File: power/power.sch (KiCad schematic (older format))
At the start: 74 parts, among them J1 Conn_01x02_Female, J2 Conn_01x02_Female, J3 CONN_02X03, J4 Conn_01x06_Female, Q1 BS170, Q11 BS170, Q12 BSB014N04LX3, Q2 BS170, Q3 BS170, Q5 BS170, Q6 BS170, Q7 BS170, U1 MAX1648, U2 TPS2592xx

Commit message: rev1 layout organization
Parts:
- removed J4, J?: Conn_01x06_Female, Connector_PinHeader_1.00mm:PinHeader_1x06_P1.00mm_Vertical, symbol Connector:Conn_01x06_Female
- added J12, J13, J14, J15, J4, J5: Conn_01x02_Female, Connector_PinHeader_1.00mm:PinHeader_1x02_P1.00mm_Vertical, symbol Connector:Conn_01x02_Female
- added TH?: Thermistor_NTC, symbol Device:Thermistor_NTC
- gave numbers to parts that had none: 22

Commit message: thermistor footprint
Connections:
- net labels removed: Discharge, SafetySwitchA, SafetySwitchB
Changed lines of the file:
@@
 Text Label 9880 2500 0    50   ~ 0
 FET1A
-Text Label 9880 3500 0    50   ~ 0
-Discharge
 Text Label 9880 2400 0    50   ~ 0
 FET2A
@@
 	1    0    0    -1
 $EndComp
-Text Label 9880 2300 0    50   ~ 0
-SafetySwitchA
 Text Label 9880 3200 0    50   ~ 0
 RESET
@@
 	5650 7170 5650 7370
 Connection ~ 5650 7370
-Text Label 9880 2900 0    50   ~ 0
-SafetySwitchB
 Text Notes 1730 3200 0    50   ~ 0
 1/10 W

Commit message: removed extra thermistor
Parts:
- removed TH?: Thermistor_NTC, symbol Device:Thermistor_NTC
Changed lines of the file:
@@
 	1    0    0    -1
 $EndComp
-$Comp
-L Device:Thermistor_NTC TH?
-U 1 1 5FFA8A9D
-P 4610 820
-F 0 "TH?" V 4320 820 50  0000 C CNN
-F 1 "Thermistor_NTC" V 4411 820 50  0000 C CNN
-F 2 "" H 4610 870 50  0001 C CNN
-F 3 "~" H 4610 870 50  0001 C CNN
-	1    4610 820
-	0    1    1    0
-$EndComp
 $EndSCHEMATC

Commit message: separated charging from main board
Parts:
- removed C10: 0.1uF, Capacitor_SMD:C_0805_2012Metric_Pad1.15x1.40mm_HandSolder, symbol Device:C_Small
- removed C11: 47uF, Capacitor_SMD:C_0805_2012Metric_Pad1.15x1.40mm_HandSolder, symbol Device:CP
- removed C2, C4: 0.1uF, Capacitor_SMD:C_0805_2012Metric_Pad1.15x1.40mm_HandSolder, symbol Device:C
- removed C3: 47nF, Capacitor_SMD:C_0805_2012Metric_Pad1.15x1.40mm_HandSolder, symbol Device:C
- removed C8: 22uF, Capacitor_SMD:C_0805_2012Metric_Pad1.15x1.40mm_HandSolder, symbol Device:CP
- removed C9: 1uF, Capacitor_SMD:C_0805_2012Metric_Pad1.15x1.40mm_HandSolder, symbol Device:C
- removed D3, D5, D6: S, footprints:SD103AW-13-F, symbol Device:D_Schottky
- removed D4: UF5400, Diode_THT:D_DO-201AD_P15.24mm_Horizontal, symbol Diode:UF5400
- removed D7: 12.5V, symbol Device:D_Zener
- removed J2: Conn_01x02_Female, Connector_PinHeader_1.00mm:PinHeader_1x02_P1.00mm_Vertical, symbol Connector:Conn_01x02_Female
- removed L1: 22uH, Inductor_SMD:L_0805_2012Metric_Pad1.15x1.40mm_HandSolder, symbol pspice:INDUCTOR
- removed Q11: BS170, Package_TO_SOT_THT:TO-92_Inline, symbol Transistor_FET:BS170
- removed Q12: BSB014N04LX3, Package_DirectFET:DirectFET_MX, symbol Transistor_FET:BSB014N04LX3
- removed R1, R2, R3, R4: R, Resistor_SMD:R_0805_2012Metric_Pad1.15x1.40mm_HandSolder, symbol Device:R
- removed R13, R5, R6: 10k, Resistor_SMD:R_0805_2012Metric_Pad1.15x1.40mm_HandSolder, symbol Device:R
- removed R15: 10, Resistor_SMD:R_0805_2012Metric_Pad1.15x1.40mm_HandSolder, symbol Device:R
- removed R22: 0.74, Resistor_SMD:R_0805_2012Metric_Pad1.15x1.40mm_HandSolder, symbol Device:R
- removed SW1: SW_Push, symbol Switch:SW_Push
- removed TH4: Thermistor, footprints:Thermistor, symbol Device:Thermistor
- removed U1: MAX1648, Package_SO:SOIC-16_3.9x9.9mm_P1.27mm, symbol Battery_Management:MAX1648
- added D3: D_Zener_13V, footprints:D_13V_Zener, symbol formula:D_Zener_13V
- added J2: Barrel_jack, footprints:barrel_jack_PJ-037A, symbol formula:Barrel_jack
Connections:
- net labels removed: DC+, DC-
- wire segments 187 -> 113
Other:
- note added: "Charging INPUT Connectors"
- note removed: "0V"
- note removed: "1.024V"
- note removed: "1.025V"
- note removed: "1/10 W"
- note removed: "10V"
- note removed: "20V"
- note removed: "3.9V"
- note removed: "35V"
- note removed: "40V"
- note removed: "Charging\n"
- note removed: "Power INPUT Connectors"
- moved on the sheet: J1, J10, J11, J12, J13, J14, J15, J3, J4, J5, J6, J7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

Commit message: half layout
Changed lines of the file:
@@
 Text Label 870  8370 2    50   ~ 0
 BAT-
-Text Label 3740 2500 0    50   ~ 0
+Text Label 3740 3400 0    50   ~ 0
 FET1A
 Text Label 3740 2400 0    50   ~ 0
 FET2A
-Text Label 3740 1700 0    50   ~ 0
+Text Label 3740 2500 0    50   ~ 0
 FET3A
 Text Label 3740 1800 0    50   ~ 0
 FET1B
-Text Label 3740 3400 0    50   ~ 0
+Text Label 3740 1700 0    50   ~ 0
 FET2B
 Text Label 3740 3300 0    50   ~ 0

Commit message: complete layout
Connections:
- net labels removed: VCC
- no-connect marks 6 -> 8
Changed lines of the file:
@@
 MOSI
-$Comp
-L power:VCC #PWR0101
-U 1 1 5E15CCC8
-P 6310 1400
-F 0 "#PWR0101" H 6310 1250 50  0001 C CNN
-F 1 "VCC" H 6327 1573 50  0000 C CNN
-F 2 "" H 6310 1400 50  0001 C CNN
-F 3 "" H 6310 1400 50  0001 C CNN
-	1    6310 1400
-	1    0    0    -1
-$EndComp
 $Comp
 L power:GND #PWR0102
@@
 	1    0    0    -1
 $EndComp
-Text Label 3740 3700 0    50   ~ 0
+Text Label 3740 3500 0    50   ~ 0
 V2A
-Text Label 3740 1600 0    50   ~ 0
+Text Label 3740 2500 0    50   ~ 0
 V3A
-Text Label 3740 1900 0    50   ~ 0
+Text Label 3740 2000 0    50   ~ 0
 V1B
-Text Label 3740 2000 0    50   ~ 0
+Text Label 3740 3000 0    50   ~ 0
 V2B
-Text Label 3740 2700 0    50   ~ 0
+Text Label 3740 1700 0    50   ~ 0
 V3B
 Wire Wire Line
@@
 Text Label 3740 2400 0    50   ~ 0
 FET2A
-Text Label 3740 2500 0    50   ~ 0
+Text Label 3740 2600 0    50   ~ 0
 FET3A
+Text Label 3740 1900 0    50   ~ 0
+FET1B
 Text Label 3740 1800 0    50   ~ 0
-FET1B
-Text Label 3740 1700 0    50   ~ 0
 FET2B
-Text Label 3740 3300 0    50   ~ 0
+Text Label 3740 2900 0    50   ~ 0
 FET3B
 Text Label 870  5620 2    50   ~ 0
@@
 	3190 5620 3890 5620
 Connection ~ 3190 5620
-Text Label 3740 3800 0    50   ~ 0
+Text Label 3740 3300 0    50   ~ 0
 V1A
 $Comp
@@
 Wire Wire Line
 	1390 3900 1390 4000
-NoConn ~ 3740 2600
 NoConn ~ 3740 2800
-NoConn ~ 3740 3000
 NoConn ~ 3740 3600
 NoConn ~ 3740 4200
@@
 	0    1    1    0
 $EndComp
+NoConn ~ 3740 1600
+NoConn ~ 3740 2300
+NoConn ~ 3740 3700
+NoConn ~ 3740 3800
+$Comp
+L power:+3.3V #PWR?
+U 1 1 5FF49F28
+P 6310 1400
+F 0 "#PWR?" H 6310 1250 50  0001 C CNN
+F 1 "+3.3V" H 6325 1573 50  0000 C CNN
+F 2 "" H 6310 1400 50  0001 C CNN
+F 3 "" H 6310 1400 50  0001 C CNN
+	1    6310 1400
+	1    0    0    -1
+$EndComp
 $EndSCHEMATC

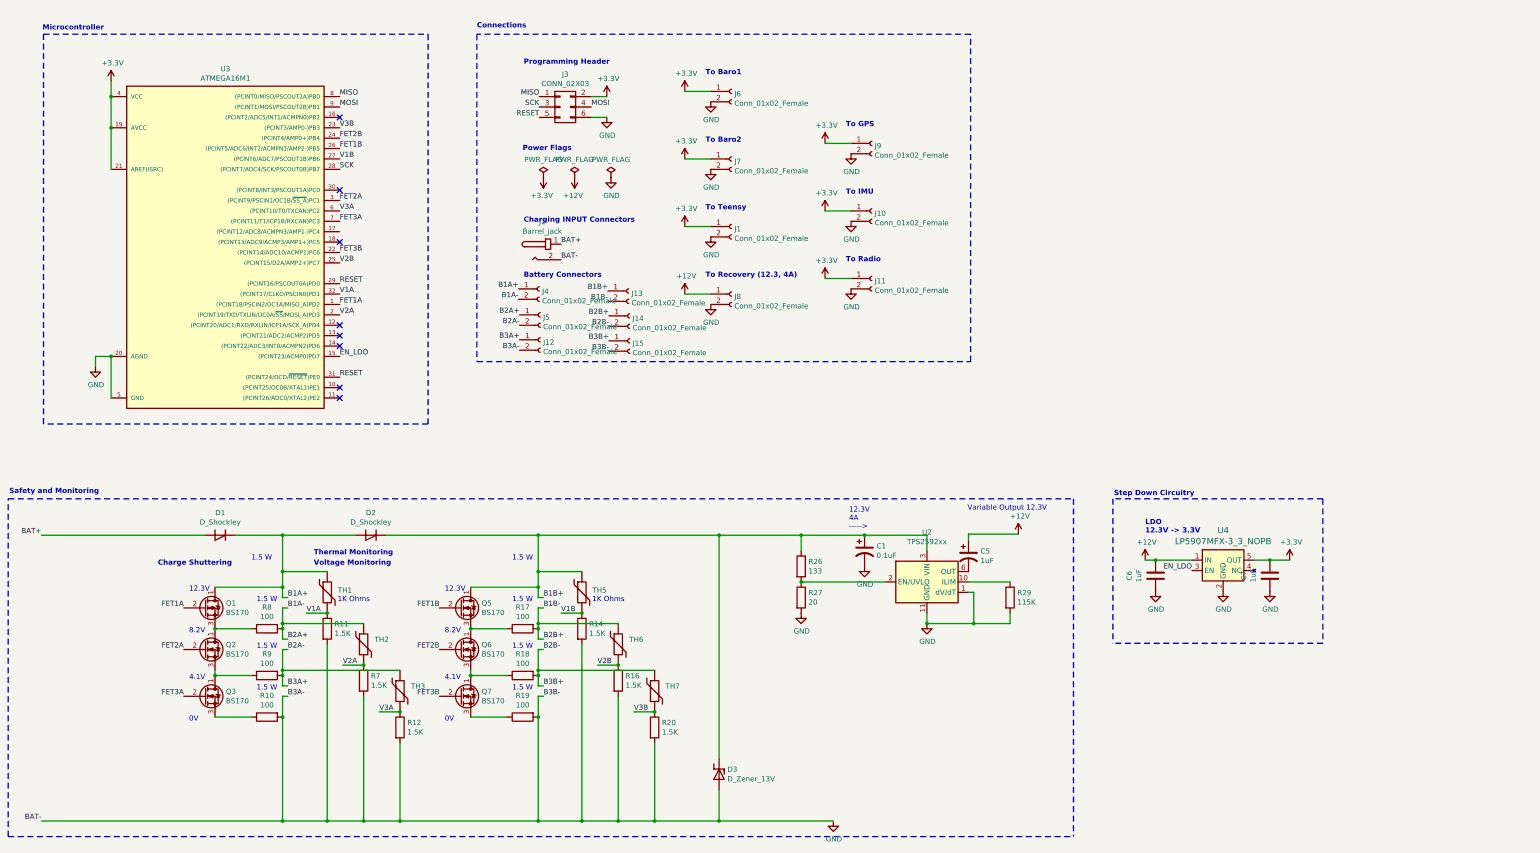
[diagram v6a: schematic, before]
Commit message: debugging LEDs, recovery
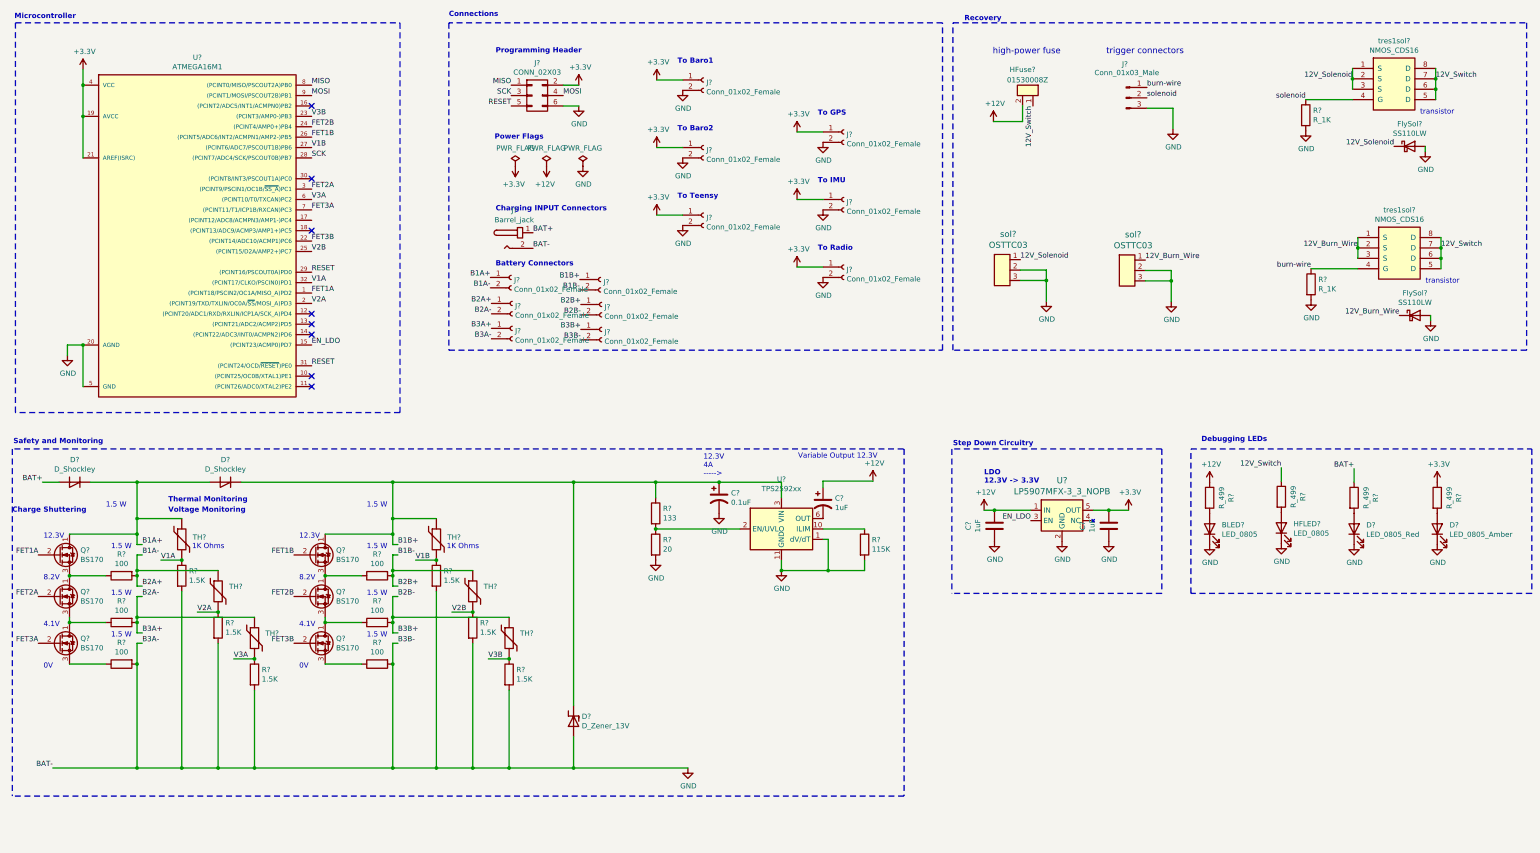
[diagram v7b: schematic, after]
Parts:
- removed J8: Conn_01x02_Female, Connector_PinHeader_1.00mm:PinHeader_1x02_P1.00mm_Vertical, symbol Connector:Conn_01x02_Female
- added BLED?, HFLED?: LED_0805, footprints:LED_0805_OEM, symbol solenoidTrigger-rescue:LED_0805-Rocketry
- added D?: LED_0805_Red, footprints:LED_0805_OEM, symbol formula:LED_0805_Red
- added D?: LED_0805_Amber, footprints:LED_0805_OEM, symbol formula:LED_0805_Amber
- added FlySol? (x2): SS110LW, footprints:D_SOD-123W_OEM, symbol solenoidTrigger-rescue:SS110LW-Rocketry
- added HFuse?: 01530008Z, footprints:01530008Z, symbol solenoidTrigger-rescue:01530008Z-Rocketry
- added J?: Conn_01x03_Male, Connector_PinHeader_2.54mm:PinHeader_1x03_P2.54mm_Vertical, symbol Connector:Conn_01x03_Male
- added R? (x4): R_499, footprints:R_0805_OEM, symbol solenoidTrigger-rescue:R_499-Rocketry
- added R? (x2): R_1K, footprints:R_0805_OEM, symbol solenoidTrigger-rescue:R_1K-Rocketry
- added sol? (x2): OSTTC03, recovery-trigger-sp20:OSTTC030162, symbol solenoidTrigger-rescue:OSTTC03-Rocketry
- added tres1sol? (x2): NMOS_CDS16, recovery-trigger-sp20:CSD16322Q5, symbol solenoidTrigger-rescue:NMOS_CDS16-Rocketry
- renumbered C6 to C?, C7 to C?, C1 to C?, C5 to C?, D1 to D?, D2 to D?, D3 to D?, J3 to J?, J1 to J?, J7 to J?, J6 to J?, J10 to J?, J9 to J?, J2 to J?, J11 to J?, J4 to J?, J5 to J?, J12 to J?, J13 to J?, J14 to J?, J15 to J?, Q1 to Q?, Q2 to Q?, Q3 to Q?, Q5 to Q?, Q7 to Q?, Q6 to Q?, R8 to R?, R9 to R?, R10 to R?, R17 to R?, R18 to R?, R19 to R?, R29 to R?, R27 to R?, R26 to R?, R11 to R?, R7 to R?, R12 to R?, R14 to R?, R16 to R?, R20 to R?, TH1 to TH?, TH2 to TH?, TH3 to TH?, TH5 to TH?, TH6 to TH?, TH7 to TH?, U2 to U?, U3 to U?, U4 to U?
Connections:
- net +12V: now also HFuse?.2, R?.1
- net +3V3: now also R?.1
- net BAT+: now also R?.1
- net GND: now also BLED?.1 (K), D?.1 (K), D?.1 (K), FlySol?.2 (A), FlySol?.2 (A), HFLED?.1 (K), J?.3 (Pin_3), R?.2, R?.2, sol?.2, sol?.2, sol?.3, sol?.3
- new net: BLED?.2 (A), R?.2
- new net: HFLED?.2 (A), R?.2
- new net: D?.2 (A), R?.2 (x2)
- new net 12V_Burn_Wire: FlySol?.1 (K), sol?.1, tres1sol?.1 (S), tres1sol?.2 (S), tres1sol?.3 (S)
- new net 12V_Solenoid: FlySol?.1 (K), sol?.1, tres1sol?.1 (S), tres1sol?.2 (S), tres1sol?.3 (S)
- new net 12V_Switch: HFuse?.1, R?.1, tres1sol?.5 (D), tres1sol?.5 (D), tres1sol?.6 (D), tres1sol?.6 (D), tres1sol?.7 (D), tres1sol?.7 (D), tres1sol?.8 (D), tres1sol?.8 (D)
- new net burn-wire: J?.1 (Pin_1), R?.1, tres1sol?.4 (G)
- new net solenoid: J?.2 (Pin_2), R?.1, tres1sol?.4 (G)
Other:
- note added: "Debugging LEDs"
- note added: "Recovery"
- note added: "high-power fuse"
- note added: "transistor"
- note added: "trigger connectors"
- note removed: "To Recovery (12.3, 4A)"
- moved on the sheet: C?, D?, J?, Q?, R?, TH?, U?

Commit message: layout complete other than missing recovery footprints
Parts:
- BLED1: renamed from BLED?; symbol solenoidTrigger-rescue:LED_0805-Rocketry -> power-rescue:LED_0805-Rocketry-solenoidTrigger-rescue
- FlySol1, FlySol2: renamed from FlySol?; symbol solenoidTrigger-rescue:SS110LW-Rocketry -> power-rescue:SS110LW-Rocketry-solenoidTrigger-rescue
- HFLED1: renamed from HFLED?; symbol solenoidTrigger-rescue:LED_0805-Rocketry -> power-rescue:LED_0805-Rocketry-solenoidTrigger-rescue
- HFuse1: renamed from HFuse?; symbol solenoidTrigger-rescue:01530008Z-Rocketry -> power-rescue:01530008Z-Rocketry-solenoidTrigger-rescue
- R16, R17, R20, R21: renamed from R?; symbol solenoidTrigger-rescue:R_499-Rocketry -> power-rescue:R_499-Rocketry-solenoidTrigger-rescue
- R18, R19: renamed from R?; symbol solenoidTrigger-rescue:R_1K-Rocketry -> power-rescue:R_1K-Rocketry-solenoidTrigger-rescue
- sol1, sol2: renamed from sol?; symbol solenoidTrigger-rescue:OSTTC03-Rocketry -> power-rescue:OSTTC03-Rocketry-solenoidTrigger-rescue
- tres1sol1, tres1sol2: renamed from tres1sol?; symbol solenoidTrigger-rescue:NMOS_CDS16-Rocketry -> power-rescue:NMOS_CDS16-Rocketry-solenoidTrigger-rescue
- gave numbers to parts that had none: 54
